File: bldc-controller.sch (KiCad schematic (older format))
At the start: 14 parts, among them U1 STM32F401CBUx

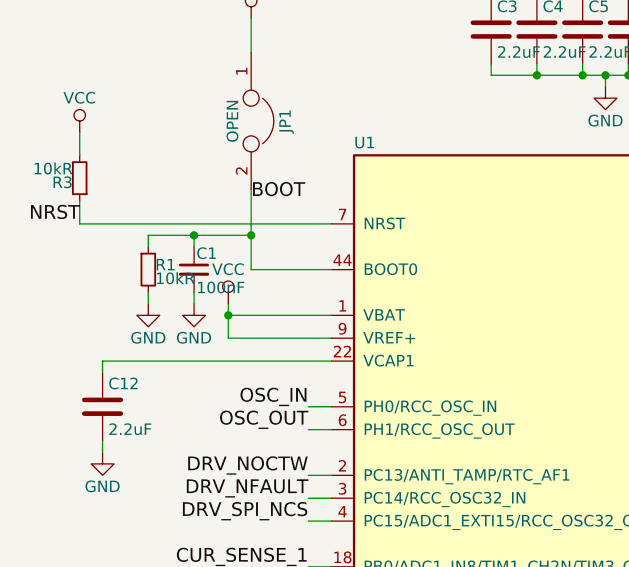
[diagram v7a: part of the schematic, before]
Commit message: well... actually we dont need those thwo parts since the bootloader can be entered from flash software
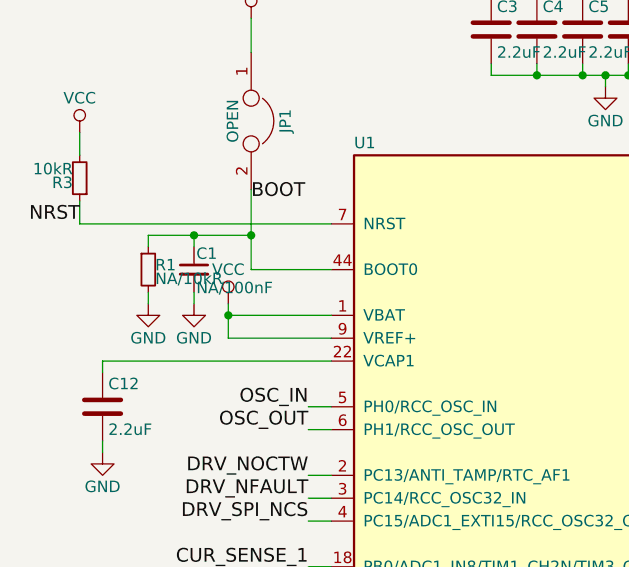
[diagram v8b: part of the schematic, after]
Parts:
- C1: value 100nF -> NA/100nF
- R1: value 10kR -> NA/10kR
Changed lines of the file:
@@
 P 1000 2050
 F 0 "R1" H 1030 2070 50  0000 L CNN
-F 1 "10kR" H 1030 2010 50  0000 L CNN
+F 1 "NA/10kR" H 1030 2010 50  0000 L CNN
 F 2 "Resistors_SMD:R_0603" H 1000 2050 50  0001 C CNN
 F 3 "" H 1000 2050 50  0000 C CNN
@@
 P 1200 2050
 F 0 "C1" H 1210 2120 50  0000 L CNN
-F 1 "100nF" H 1210 1970 50  0000 L CNN
+F 1 "NA/100nF" H 1210 1970 50  0000 L CNN
 F 2 "Capacitors_SMD:C_0603" H 1200 2050 50  0001 C CNN
 F 3 "" H 1200 2050 50  0000 C CNN
